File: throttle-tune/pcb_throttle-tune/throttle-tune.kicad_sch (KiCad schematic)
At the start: 31 parts, among them IC1 ATMEGA8A-P, J1 Screw_Terminal_01x03, J2 Screw_Terminal_01x03, J3 Screw_Terminal_01x03, J4 Screw_Terminal_01x03, J5 Conn_01x03_Pin, J6 UART, P1 ISP, U2 LM358N

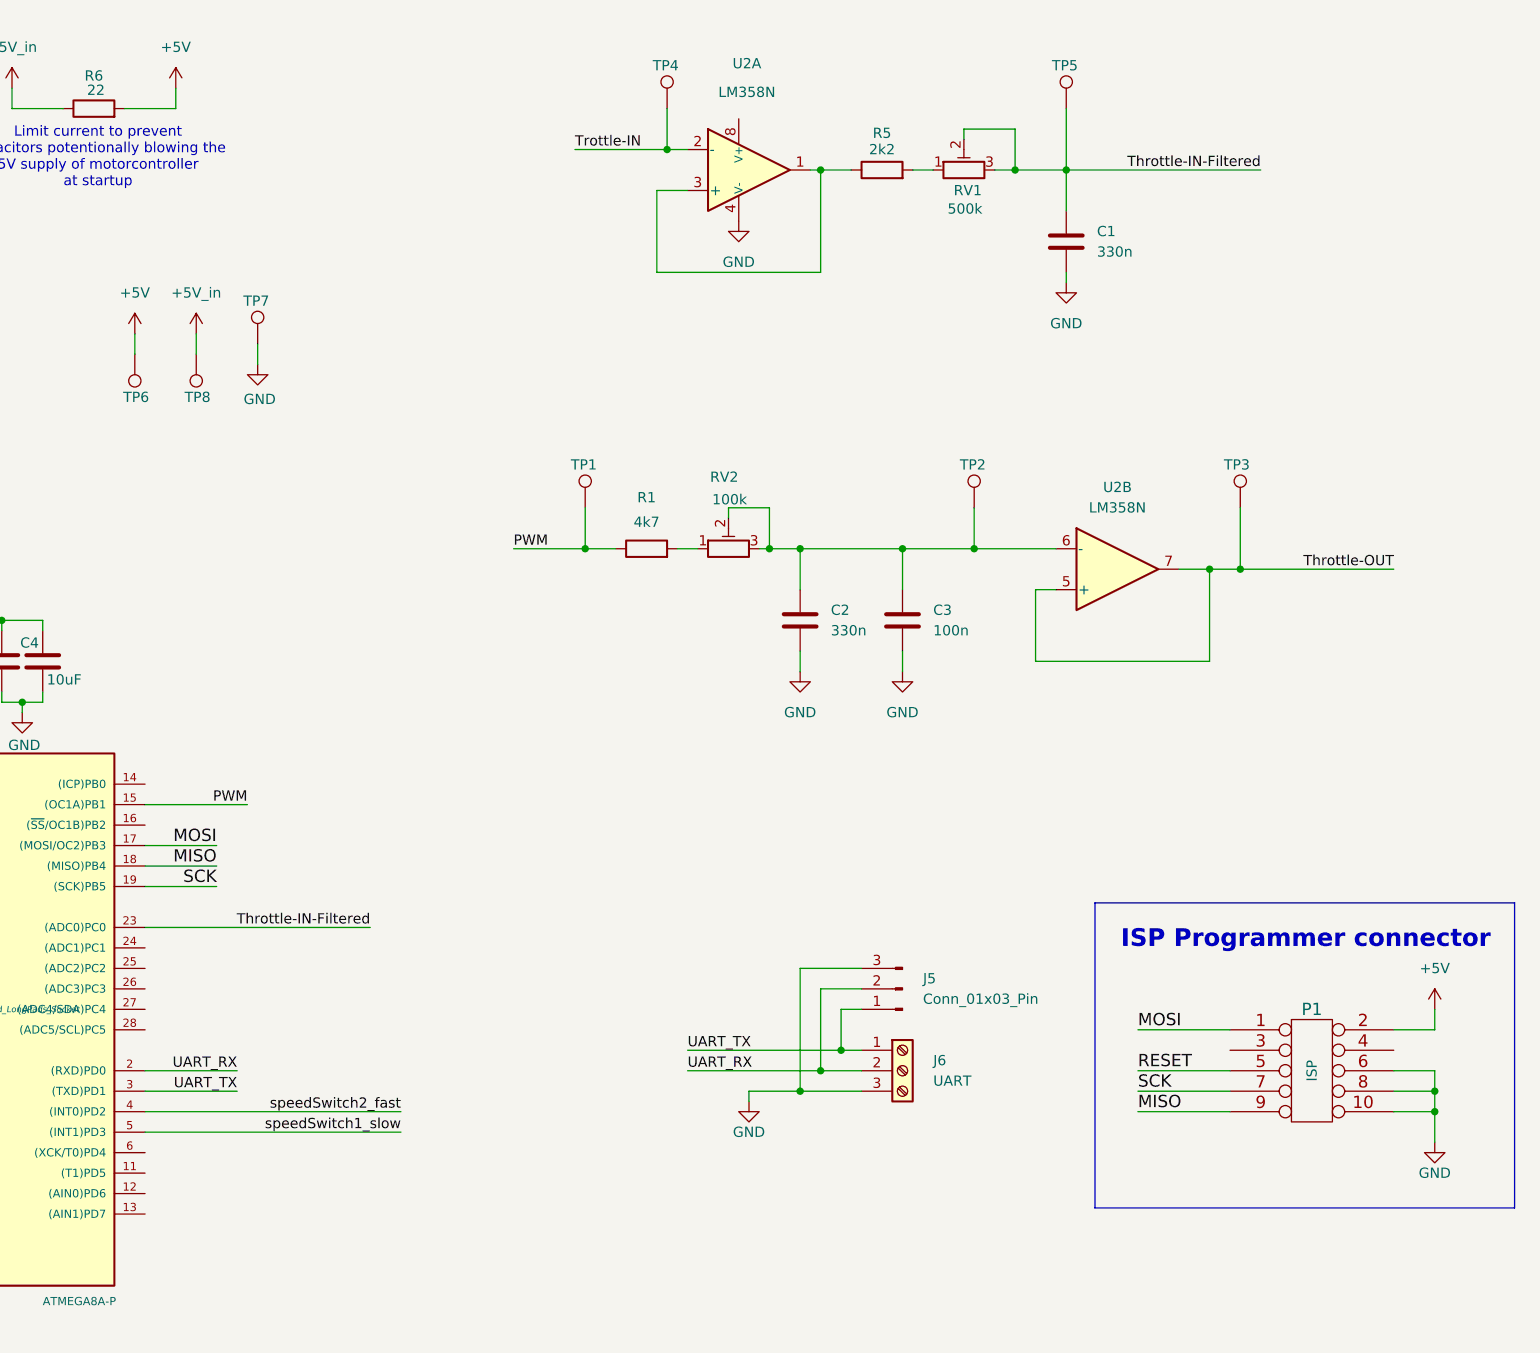
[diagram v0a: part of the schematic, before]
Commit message: pcb: schematic using supply motorcontroller (dropped)
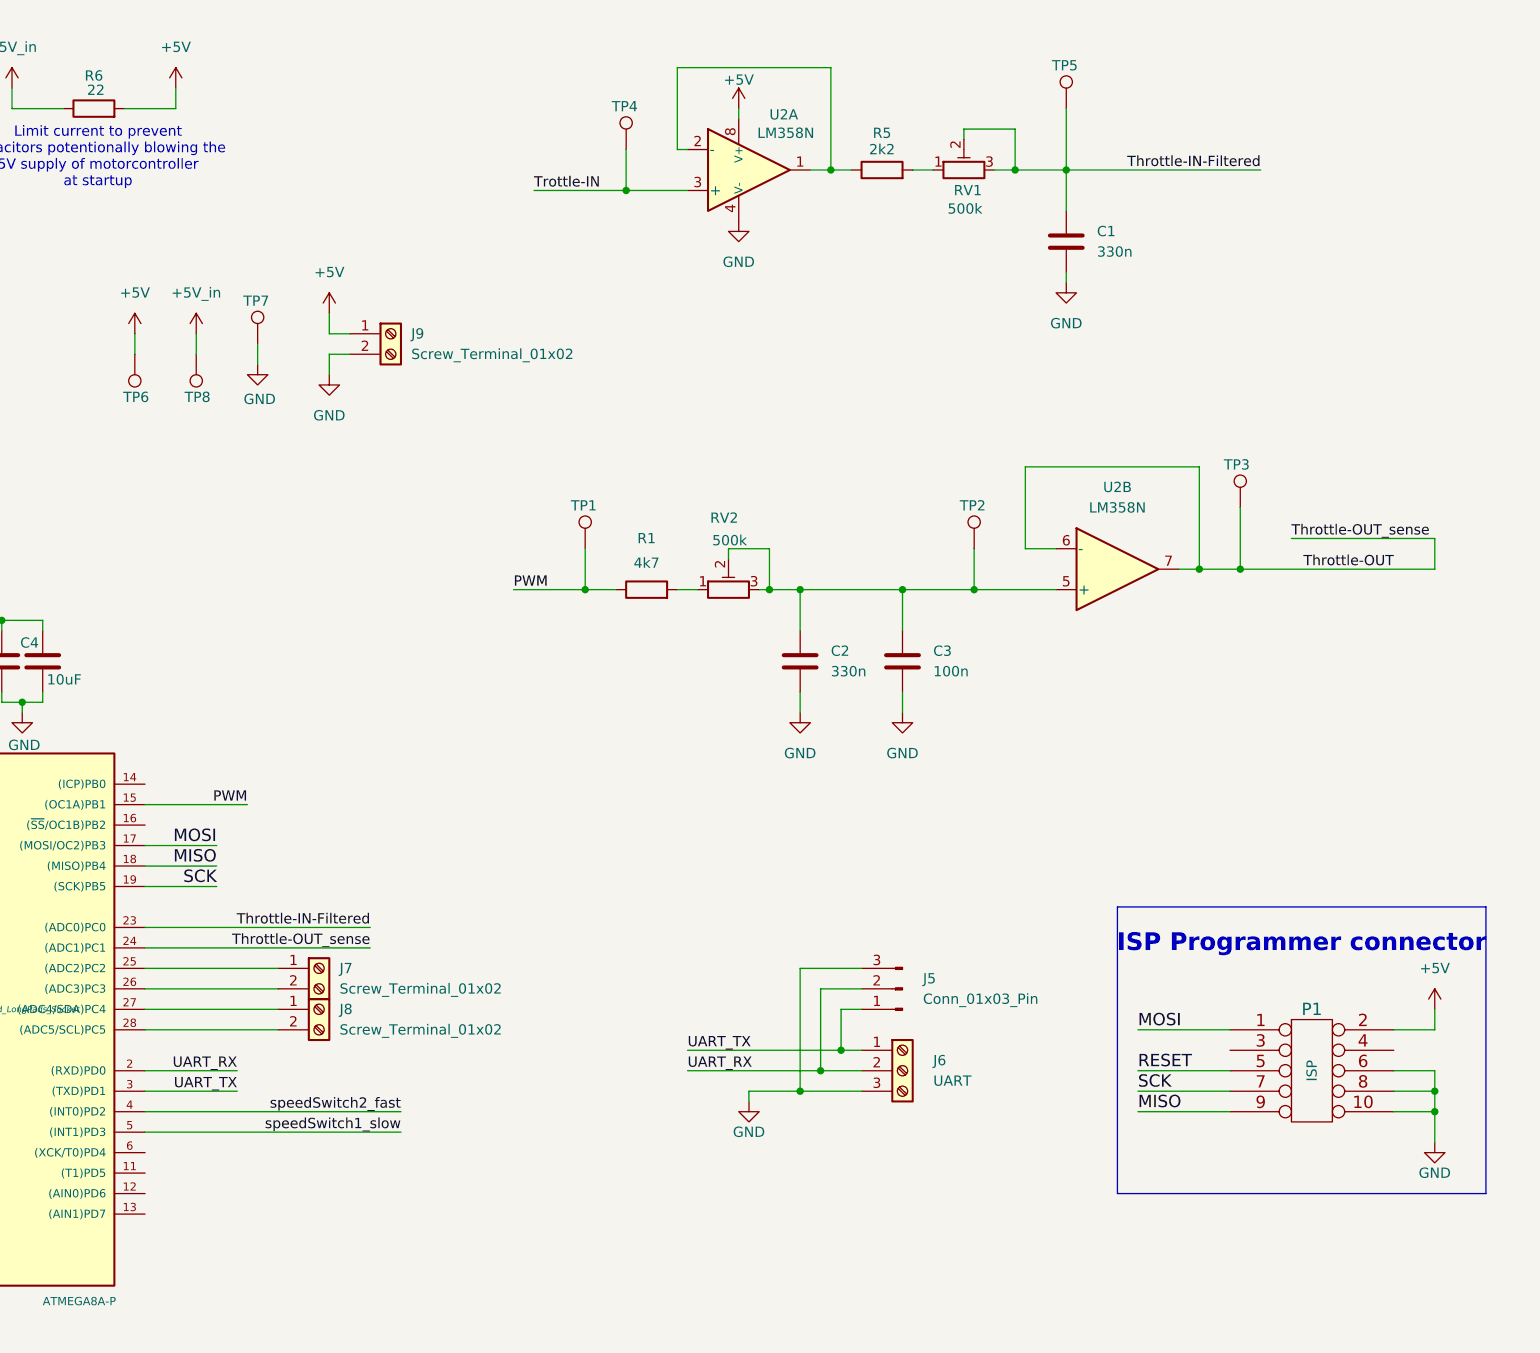
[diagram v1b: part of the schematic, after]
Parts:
- added J7, J8, J9: Screw_Terminal_01x02, symbol Connector:Screw_Terminal_01x02
- RV2: value 100k -> 500k
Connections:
- net +5V: now also U2.8 (V+), J9.1 (Pin_1)
- net GND: now also J9.2 (Pin_2)
- net Throttle-OUT: now also IC1.24 ((ADC1)PC1), U2.6 (-); no longer U2.5 (+)
- net Trottle-IN: now also U2.3 (+); no longer U2.2 (-)
- net at C2.1, C3.1, RV2.2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: now also U2.5 (+); no longer U2.6 (-)
- net at R5.1, U2.1: now also U2.2 (-); no longer U2.3 (+)
- net at IC1.25 ((ADC2)PC2): now also J7.1 (Pin_1)
- net at IC1.26 ((ADC3)PC3): now also J7.2 (Pin_2)
- net at IC1.27 ((ADC4/SDA)PC4): now also J8.1 (Pin_1)
- net at IC1.28 ((ADC5/SCL)PC5): now also J8.2 (Pin_2)
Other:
- moved on the sheet: C2, C3, R1, RV2, TP1, TP2, TP4

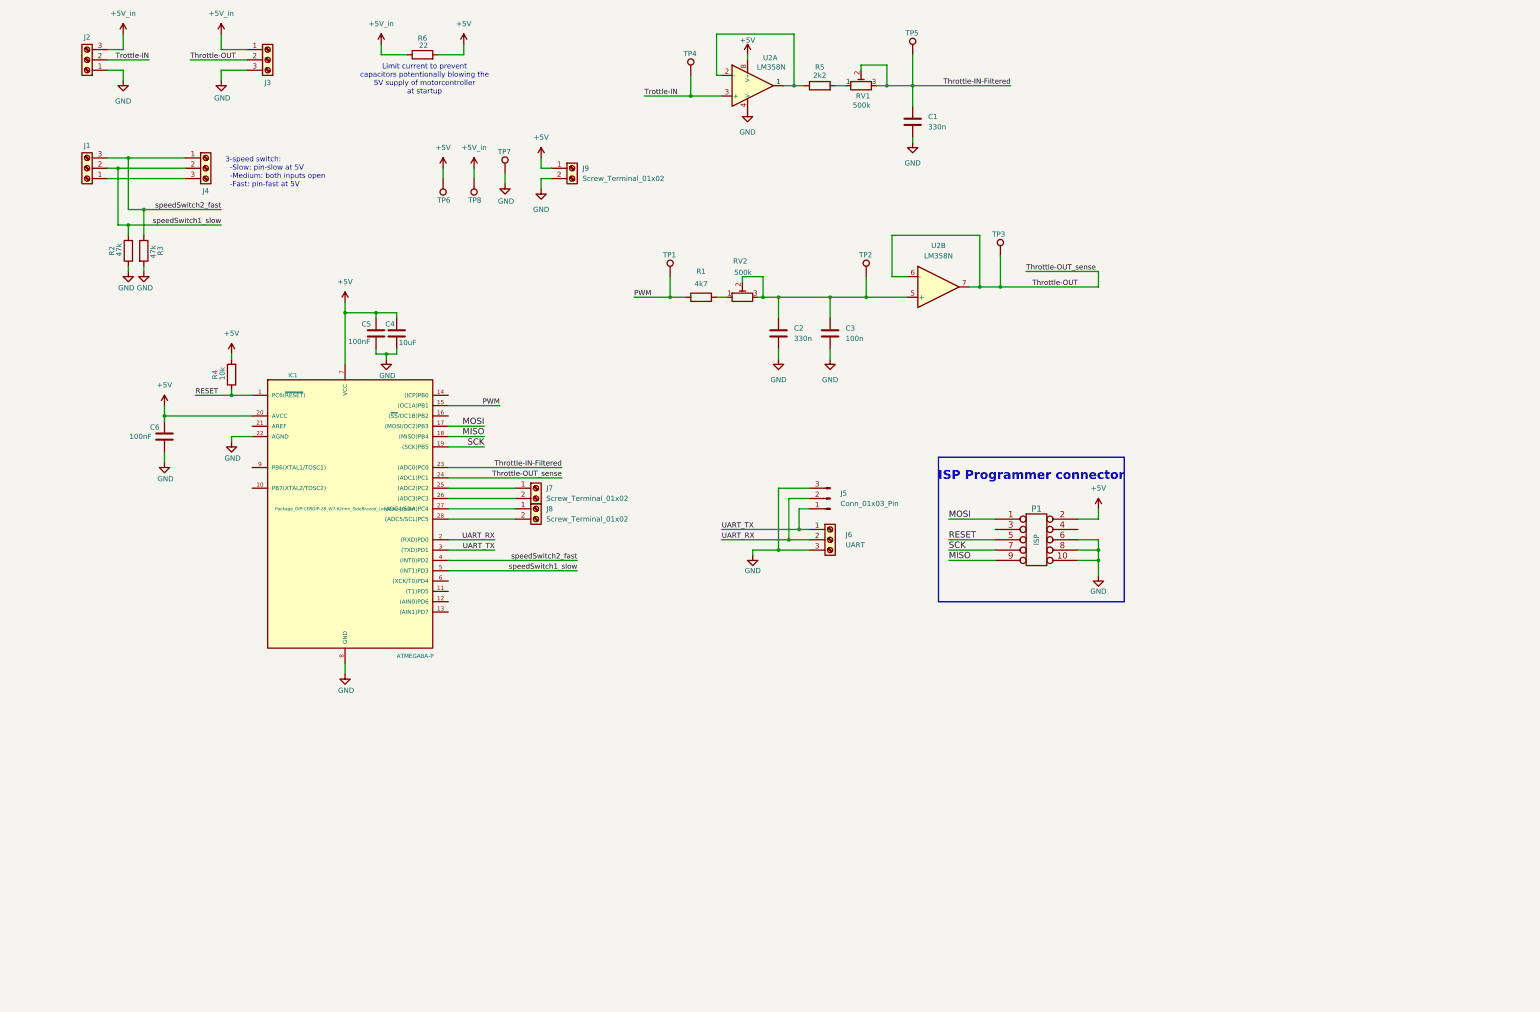
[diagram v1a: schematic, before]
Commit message: pcb: finish schematic (9V, cut-suppy, filters)
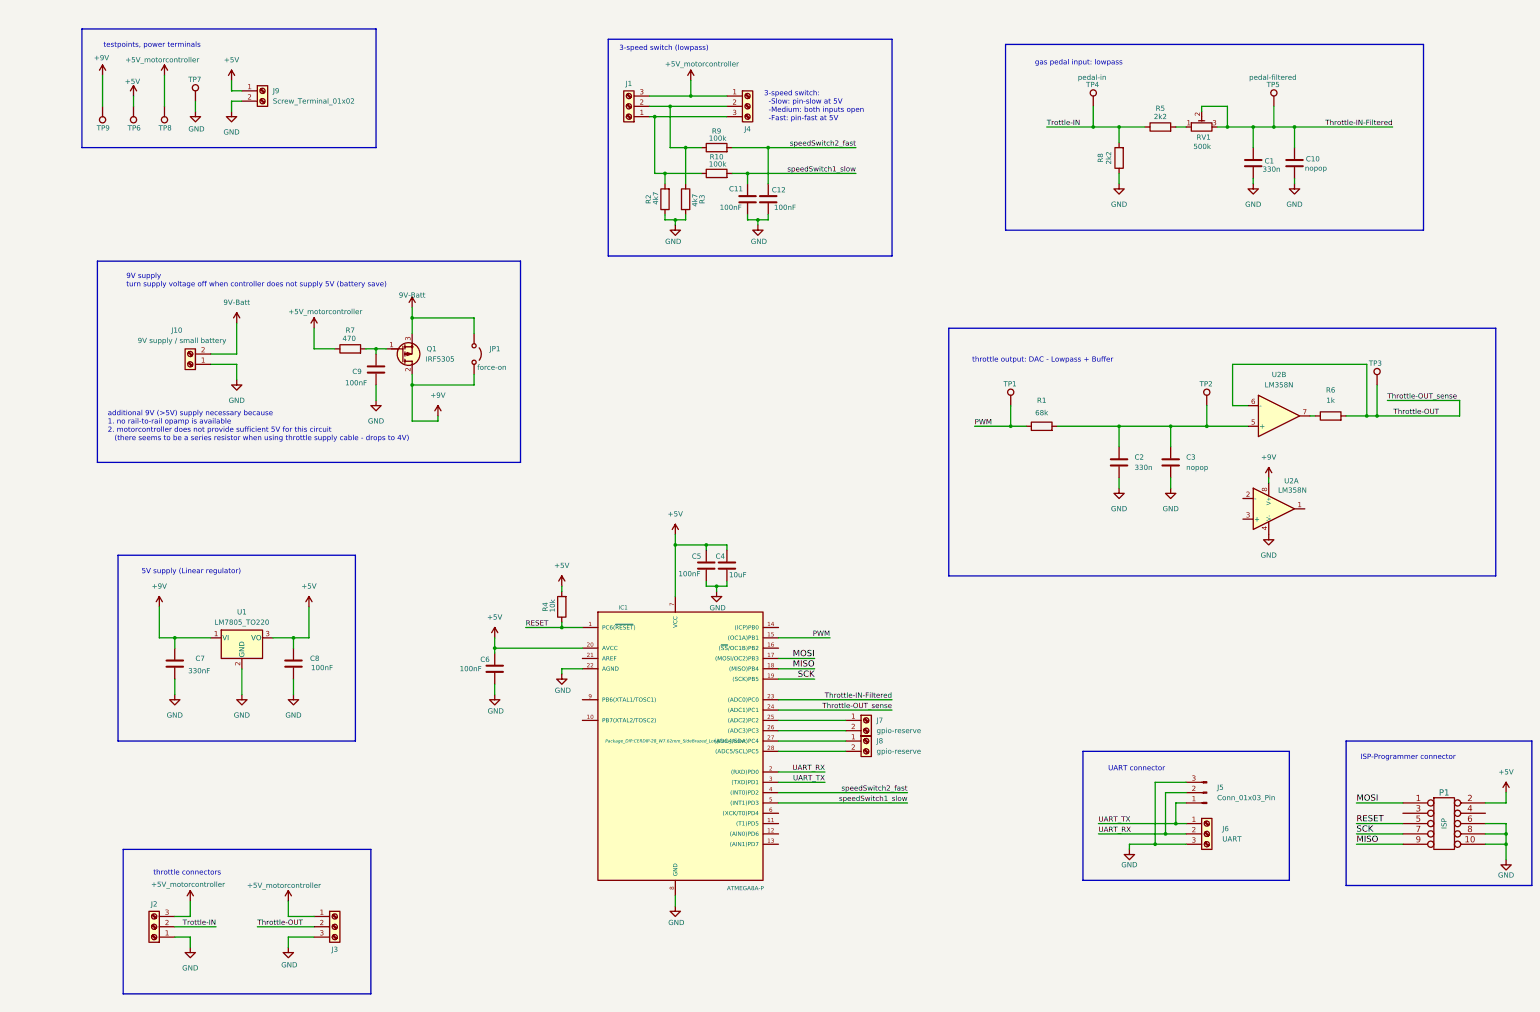
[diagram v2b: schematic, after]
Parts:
- removed RV2: 500k, symbol Device:R_Potentiometer_Trim
- added C10: nopop, Capacitor_THT:C_Disc_D8.0mm_W5.0mm_P5.00mm, symbol Device:C
- added C11, C12, C8, C9: 100nF, Capacitor_THT:C_Disc_D7.0mm_W2.5mm_P5.00mm, symbol Device:C
- added C7: 330nF, Capacitor_THT:C_Disc_D8.0mm_W5.0mm_P5.00mm, symbol Device:C
- added J10: 9V supply / small battery, TerminalBlock:TerminalBlock_bornier-2_P5.08mm, symbol Connector:Screw_Terminal_01x02
- added JP1: force-on, Connector_PinHeader_1.00mm:PinHeader_1x02_P1.00mm_Vertical, symbol Jumper:Jumper_2_Open
- added Q1: IRF5305, Package_TO_SOT_THT:TO-220F-3_Vertical, symbol Transistor_MOSFET_AKL:IRF5305
- added R10, R9: 100k, Resistor_THT:R_Axial_DIN0207_L6.3mm_D2.5mm_P10.16mm_Horizontal, symbol Device:R
- added R7: 470, Resistor_THT:R_Axial_DIN0207_L6.3mm_D2.5mm_P10.16mm_Horizontal, symbol Device:R
- added R8: 2k2, Resistor_THT:R_Axial_DIN0207_L6.3mm_D2.5mm_P10.16mm_Horizontal, symbol Device:R
- added TP9: TestPoint, Connector_PinHeader_1.00mm:PinHeader_1x01_P1.00mm_Vertical, symbol Connector:TestPoint
- added U1: LM7805_TO220, Package_TO_SOT_THT:TO-220-3_Vertical, symbol Regulator_Linear:LM7805_TO220
- C1, C2: footprint (none) -> Capacitor_THT:C_Disc_D8.0mm_W5.0mm_P5.00mm
- C3: value 100n -> nopop; footprint (none) -> Capacitor_THT:C_Disc_D8.0mm_W5.0mm_P5.00mm
- C4: footprint (none) -> Capacitor_THT:CP_Radial_D5.0mm_P2.50mm
- C5, C6: footprint (none) -> Capacitor_THT:C_Disc_D7.0mm_W2.5mm_P5.00mm
- J1, J2, J3, J4: footprint (none) -> TerminalBlock:TerminalBlock_bornier-3_P5.08mm
- J5: footprint (none) -> Connector_PinHeader_1.00mm:PinHeader_1x03_P1.00mm_Vertical
- J6, J9: footprint (none) -> TerminalBlock:TerminalBlock_bornier-2_P5.08mm
- J7, J8: value Screw_Terminal_01x02 -> gpio-reserve; footprint (none) -> TerminalBlock:TerminalBlock_bornier-2_P5.08mm
- R1: value 4k7 -> 68k; footprint (none) -> Resistor_THT:R_Axial_DIN0207_L6.3mm_D2.5mm_P10.16mm_Horizontal
- R2, R3: value 47k -> 4k7; footprint (none) -> Resistor_THT:R_Axial_DIN0207_L6.3mm_D2.5mm_P10.16mm_Horizontal
- R4, R5, RV1: footprint (none) -> Resistor_THT:R_Axial_DIN0207_L6.3mm_D2.5mm_P10.16mm_Horizontal
- R6: value 22 -> 1k; footprint (none) -> Resistor_THT:R_Axial_DIN0207_L6.3mm_D2.5mm_P10.16mm_Horizontal
- TP1, TP2, TP3, TP6, TP7, TP8: footprint (none) -> Connector_PinHeader_1.00mm:PinHeader_1x01_P1.00mm_Vertical
- TP4: value TestPoint -> pedal-in; footprint (none) -> Connector_PinHeader_1.00mm:PinHeader_1x01_P1.00mm_Vertical
- TP5: value TestPoint -> pedal-filtered; footprint (none) -> Connector_PinHeader_1.00mm:PinHeader_1x01_P1.00mm_Vertical
- U2: footprint Package_DIP_AKL:DIP-8_W7.62mm_LongPads -> Package_DIP:DIP-8_W7.62mm_LongPads
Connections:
- net +5V: now also C8.1, U1.3 (VO); no longer R6.2, U2.8 (V+)
- net GND: now also C10.2, C11.2, C12.2, C7.2, C8.2, C9.2, J10.1 (Pin_1), R8.1, U1.2 (GND)
- net Throttle-IN-Filtered: now also C10.1
- net Throttle-OUT: now also R6.2; no longer U2.7
- net Trottle-IN: now also R5.1, R8.2; no longer U2.3 (+)
- net speedSwitch1_slow: now also C11.1, R10.2; no longer J1.2 (Pin_2), J4.2 (Pin_2), R2.2
- net speedSwitch2_fast: now also C12.1, R9.2; no longer J1.3 (Pin_3), J4.1 (Pin_1), R3.1
- net at C2.1, C3.1, TP2.1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: now also R1.2
- net at J1.1 (Pin_1), J4.3 (Pin_3): now also R2.2, R10.1
- net +5V_in renamed +5V_motorcontroller
- net +5V_motorcontroller: now also J1.3 (Pin_3), J4.1 (Pin_1), R7.1; no longer R6.1
- new net: R6.1, U2.7
- new net: C9.1, Q1.1 (G), R7.2
- new net: J1.2 (Pin_2), J4.2 (Pin_2), R3.1, R9.1
- new net +9V: C7.1, JP1.2 (B), Q1.2 (D), TP9.1, U1.1 (VI), U2.8 (V+)
- new net 9V-Batt: J10.2 (Pin_2), JP1.1 (A), Q1.3 (S)
- now unconnected: U2.1, U2.2 (-)
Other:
- note added: "3-speed switch (lowpass)"
- note added: "5V supply (Linear regulator)"
- note added: "9V supply turn supply voltage off when controller does not supply 5V (battery save)"
- note added: "ISP-Programmer connector"
- note added: "UART connector"
- note added: "additional 9V (>5V) supply necessary because 1. no rail-to-rail opamp is available 2. motorcontroller does not provide sufficient 5V for this circuit (there seems to be a series resistor when using throttle supply cable - drops to 4V)"
- note added: "gas pedal input: lowpass"
- note added: "testpoints, power terminals"
- note added: "throttle connectors"
- note added: "throttle output: DAC - Lowpass + Buffer"
- note removed: "ISP Programmer connector"
- note removed: "Limit current to prevent capacitors potentionally blowing the 5V supply of motorcontroller at startup"
- moved on the sheet: C1, C2, C3, C4, C5, C6, IC1, J1, J2, J3, J4, J5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
